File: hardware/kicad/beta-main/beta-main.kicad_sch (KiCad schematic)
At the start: 0 parts

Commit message: tweaks and added servo controller
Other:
- sheet CM5 ports: added 12V; removed none
- sheet PSU ports: added 12V; removed none
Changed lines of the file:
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@@
+	(wire
+		(pts
+			(xy 73.66 49.53) (xy 93.98 49.53)
+		)
+		(stroke
+			(width 0)
+			(type default)
+		)
+	)
 	(wire
 		(pts
@@
 			)
 		)
+		(pin "12V" output
+			(at 73.66 49.53 0)
+			(effects
+				(font
+					(size 1.27 1.27)
+				)
+				(justify right)
+			)
+		)
 		(instances
 			(project "beta-main"
@@
 			(effects
 				(font
+					(size 1.27 1.27)
+				)
+				(justify left)
+			)
+		)
+		(pin "12V" input
+			(at 93.98 49.53 180)
+			(effects
+				(font

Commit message: sync changes after meeting
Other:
- added sheet Servo Controller (servo_controller.kicad_sch)
- sheet CM5 ports: added UART3_RX, UART3_TX; removed none
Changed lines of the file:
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@@
 	(wire
 		(pts
-			(xy 68.58 69.85) (xy 68.58 72.39)
-		)
-		(stroke
-			(width 0)
-			(type default)
-		)
-	)
-	(wire
-		(pts
-			(xy 73.66 49.53) (xy 93.98 49.53)
-		)
-		(stroke
-			(width 0)
-			(type default)
-		)
-	)
-	(wire
-		(pts
-			(xy 73.66 57.15) (xy 93.98 57.15)
+			(xy 41.91 49.53) (xy 41.91 52.07)
+		)
+		(stroke
+			(width 0)
+			(type default)
+		)
+	)
+	(wire
+		(pts
+			(xy 46.99 36.83) (xy 49.53 36.83)
+		)
+		(stroke
+			(width 0)
+			(type default)
+		)
+	)
+	(wire
+		(pts
+			(xy 46.99 33.02) (xy 49.53 33.02)
+		)
+		(stroke
+			(width 0)
+			(type default)
+		)
+	)
+	(wire
+		(pts
+			(xy 46.99 29.21) (xy 49.53 29.21)
+		)
+		(stroke
+			(width 0)
+			(type default)
+		)
+	)
+	(wire
+		(pts
+			(xy 128.27 50.8) (xy 142.24 50.8)
+		)
+		(stroke
+			(width 0)
+			(type default)
+		)
+	)
+	(wire
+		(pts
+			(xy 128.27 54.61) (xy 142.24 54.61)
 		)
 		(stroke
@@
 		)
 	)
-	(wire
-		(pts
-			(xy 73.66 53.34) (xy 93.98 53.34)
-		)
-		(stroke
-			(width 0)
-			(type default)
+	(label "3V3"
+		(at 49.53 36.83 0)
+		(effects
+			(font
+				(size 1.27 1.27)
+			)
+			(justify left bottom)
+		)
+	)
+	(label "5V"
+		(at 49.53 33.02 0)
+		(effects
+			(font
+				(size 1.27 1.27)
+			)
+			(justify left bottom)
+		)
+	)
+	(label "12V"
+		(at 49.53 29.21 0)
+		(effects
+			(font
+				(size 1.27 1.27)
+			)
+			(justify left bottom)
 		)
 	)
@@
 	(symbol
 		(lib_id "power:GND")
-		(at 68.58 72.39 0)
+		(at 41.91 52.07 0)
 		(unit 1)
 		(exclude_from_sim no)
@@
 		(fields_autoplaced yes)
 		(property "Reference" "#PWR02"
-			(at 68.58 78.74 0)
+			(at 41.91 58.42 0)
 			(effects
 				(font
@@
 		)
 		(property "Value" "GND"
-			(at 68.58 77.47 0)
+			(at 41.91 57.15 0)
 			(effects
 				(font
@@
 		)
 		(property "Footprint" ""
-			(at 68.58 72.39 0)
+			(at 41.91 52.07 0)
 			(effects
 				(font
@@
 		)
 		(property "Datasheet" ""
-			(at 68.58 72.39 0)
+			(at 41.91 52.07 0)
 			(effects
 				(font
@@
 		)
 		(property "Description" "Power symbol creates a global label with name \"GND\" , ground"
-			(at 68.58 72.39 0)
+			(at 41.91 52.07 0)
 			(effects
 				(font
@@
 	)
 	(sheet
-		(at 46.99 45.72)
+		(at 20.32 25.4)
 		(size 26.67 24.13)
 		(exclude_from_sim no)
@@
 		)
 		(property "Sheetname" "PSU"
-			(at 46.99 45.0084 0)
+			(at 20.32 24.6884 0)
 			(effects
 				(font
@@
 		)
 		(property "Sheetfile" "psu.kicad_sch"
-			(at 46.99 70.4346 0)
+			(at 20.32 50.1146 0)
 			(effects
 				(font
@@
 		)
 		(pin "GND" passive
-			(at 68.58 69.85 270)
+			(at 41.91 49.53 270)
 			(effects
 				(font
@@
 		)
 		(pin "5V" output
-			(at 73.66 53.34 0)
+			(at 46.99 33.02 0)
 			(effects
 				(font
@@
 		)
 		(pin "3V3" output
-			(at 73.66 57.15 0)
+			(at 46.99 36.83 0)
 			(effects
 				(font
@@
 		)
 		(pin "12V" output
-			(at 73.66 49.53 0)
+			(at 46.99 29.21 0)
 			(effects
 				(font
@@
 			)
 		)
+		(pin "UART3_RX" input
+			(at 128.27 54.61 0)
+			(effects
+				(font
+					(size 1.27 1.27)
+				)
+				(justify right)
+			)
+		)
+		(pin "UART3_TX" input
+			(at 128.27 50.8 0)
+			(effects
+				(font
+					(size 1.27 1.27)
+				)
+				(justify right)
+			)
+		)
 		(instances
 			(project "beta-main"
@@
 				)
 			)
+		)
+	)
+	(sheet
+		(at 142.24 45.72)
+		(size 34.29 22.86)
+		(exclude_from_sim no)
+		(in_bom yes)
+		(on_board yes)
+		(dnp no)
+		(fields_autoplaced yes)
+		(stroke
+			(width 0.1524)
+			(type solid)
+		)
+		(fill
+			(color 0 0 0 0.0000)
+		)
+		(property "Sheetname" "Servo Controller"
+			(at 142.24 45.0084 0)
+			(effects
+				(font
+					(size 1.27 1.27)
+				)
+				(justify left bottom)
+			)
+		)
+		(property "Sheetfile" "servo_controller.kicad_sch"
+			(at 142.24 69.1646 0)
+			(effects
+				(font
+					(size 1.27 1.27)
+				)
+				(justify left top)
+			)
+		)
+		(pin "3V3" input
+			(at 142.24 64.77 180)
+			(effects
+				(font
+					(size 1.27 1.27)
+				)
+				(justify left)
+			)
+		)
+		(pin "12V" input
+			(at 142.24 62.23 180)
+			(effects
+				(font
+					(size 1.27 1.27)
+				)
+				(justify left)
+			)
+		)
+		(pin "GND" input
+			(at 170.18 68.58 270)
+			(effects
+				(font
+					(size 1.27 1.27)
+				)
+				(justify left)
+			)
+		)
+		(pin "UART_RX" input
+			(at 142.24 54.61 180)
+			(effects
+				(font
+					(size 1.27 1.27)
+				)
+				(justify left)
+			)
+		)
+		(pin "UART_TX" input
+			(at 142.24 50.8 180)
+			(effects
+				(font
+					(size 1.27 1.27)
+				)
+				(justify left)
+			)
+		)
+		(instances
+			(project "beta-main"
+				(path "/ec75fd42-4efa-4f32-b57e-76d632cb46f5"
+					(page "10")
+				)
+			)

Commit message: Wzmacniacz dodany
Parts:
- added U4: MAX98357A, Package_DFN_QFN:TQFN-16-1EP_3x3mm_P0.5mm_EP1.23x1.23mm, symbol Audio:MAX98357A
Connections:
- new net: U4.10 (OUTN), U4.9 (OUTP)
- new net: U4.11 (GND), U4.15 (GND), U4.3 (GND)
- new net: U4.7 (VDD), U4.8 (VDD)
- new net CM5/GPIO18: U4.16 (BCLK)
- new net CM5/GPIO19: U4.14 (LRCLK)
- new net CM5/GPIO21: U4.1 (DIN)
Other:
- sheet CM5 ports: added GPIO18, GPIO19, GPIO21; removed none
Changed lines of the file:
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@@
+	(wire
+		(pts
+			(xy 109.22 41.91) (xy 109.22 45.72)
+		)
+		(stroke
+			(width 0)
+			(type default)
+		)
+	)
 	(wire
 		(pts
@@
 	(wire
 		(pts
+			(xy 104.14 12.7) (xy 101.6 12.7)
+		)
+		(stroke
+			(width 0)
+			(type default)
+		)
+	)
+	(wire
+		(pts
 			(xy 46.99 33.02) (xy 49.53 33.02)
 		)
@@
 	(wire
 		(pts
+			(xy 106.68 38.1) (xy 106.68 41.91)
+		)
+		(stroke
+			(width 0)
+			(type default)
+		)
+	)
+	(wire
+		(pts
+			(xy 104.14 38.1) (xy 104.14 43.18)
+		)
+		(stroke
+			(width 0)
+			(type default)
+		)
+	)
+	(wire
+		(pts
+			(xy 101.6 38.1) (xy 101.6 45.72)
+		)
+		(stroke
+			(width 0)
+			(type default)
+		)
+	)
+	(wire
+		(pts
 			(xy 46.99 29.21) (xy 49.53 29.21)
 		)
@@
 	(wire
 		(pts
+			(xy 109.22 41.91) (xy 106.68 41.91)
+		)
+		(stroke
+			(width 0)
+			(type default)
+		)
+	)
+	(wire
+		(pts
 			(xy 128.27 50.8) (xy 142.24 50.8)
 		)
@@
 		(pts
 			(xy 128.27 54.61) (xy 142.24 54.61)
+		)
+		(stroke
+			(width 0)
+			(type default)
+		)
+	)
+	(wire
+		(pts
+			(xy 105.41 43.18) (xy 104.14 43.18)
+		)
+		(stroke
+			(width 0)
+			(type default)
+		)
+	)
+	(wire
+		(pts
+			(xy 105.41 43.18) (xy 105.41 45.72)
 		)
 		(stroke
@@
 			)
 			(justify left bottom)
+		)
+	)
+	(symbol
+		(lib_id "Audio:MAX98357A")
+		(at 109.22 25.4 90)
+		(unit 1)
+		(exclude_from_sim no)
+		(in_bom yes)
+		(on_board yes)
+		(dnp no)
+		(fields_autoplaced yes)
+		(property "Reference" "U4"
+			(at 92.71 19.9546 90)
+			(effects
+				(font
+					(size 1.27 1.27)
+				)
+			)
+		)
+		(property "Value" "MAX98357A"
+			(at 92.71 22.4946 90)
+			(effects
+				(font
+					(size 1.27 1.27)
+				)
+			)
+		)
+		(property "Footprint" "Package_DFN_QFN:TQFN-16-1EP_3x3mm_P0.5mm_EP1.23x1.23mm"
+			(at 111.76 26.67 0)
+			(effects
+				(font
+					(size 1.27 1.27)
+				)
+				(hide yes)
+			)
+		)
+		(property "Datasheet" "https://www.analog.com/media/en/technical-documentation/data-sheets/MAX98357A-MAX98357B.pdf"
+			(at 111.76 25.4 0)
+			(effects
+				(font
+					(size 1.27 1.27)
+				)
+				(hide yes)
+			)
+		)
+		(property "Description" "Mono DAC with amplifier, I2S, PCM, TDM, 32-bit, 96khz, 3.2W, TQFP-16"
+			(at 109.22 25.4 0)
+			(effects
+				(font
+					(size 1.27 1.27)
+				)
+				(hide yes)
+			)
+		)
+		(pin "10"
+		)
+		(pin "7"
+		)
+		(pin "17"
+		)
+		(pin "11"
+		)
+		(pin "5"
+		)
+		(pin "2"
+		)
+		(pin "15"
+		)
+		(pin "8"
+		)
+		(pin "9"
+		)
+		(pin "4"
+		)
+		(pin "14"
+		)
+		(pin "16"
+		)
+		(pin "1"
+		)
+		(pin "13"
+		)
+		(pin "12"
+		)
+		(pin "6"
+		)
+		(pin "3"
+		)
+		(instances
+			(project ""
+				(path "/ec75fd42-4efa-4f32-b57e-76d632cb46f5"
+					(reference "U4")
+					(unit 1)
+				)
+			)
 		)
 	)
@@
 			(effects
 				(font
+					(size 1.27 1.27)
+				)
+				(justify right)
+			)
+		)
+		(pin "GPIO18" input
+			(at 105.41 45.72 90)
+			(effects
+				(font
+					(size 1.27 1.27)
+				)
+				(justify right)
+			)
+		)
+		(pin "GPIO19" input
+			(at 109.22 45.72 90)
+			(effects
+				(font
+					(size 1.27 1.27)
+				)
+				(justify right)
+			)
+		)
+		(pin "GPIO21" input
+			(at 101.6 45.72 90)
+			(effects
+				(font

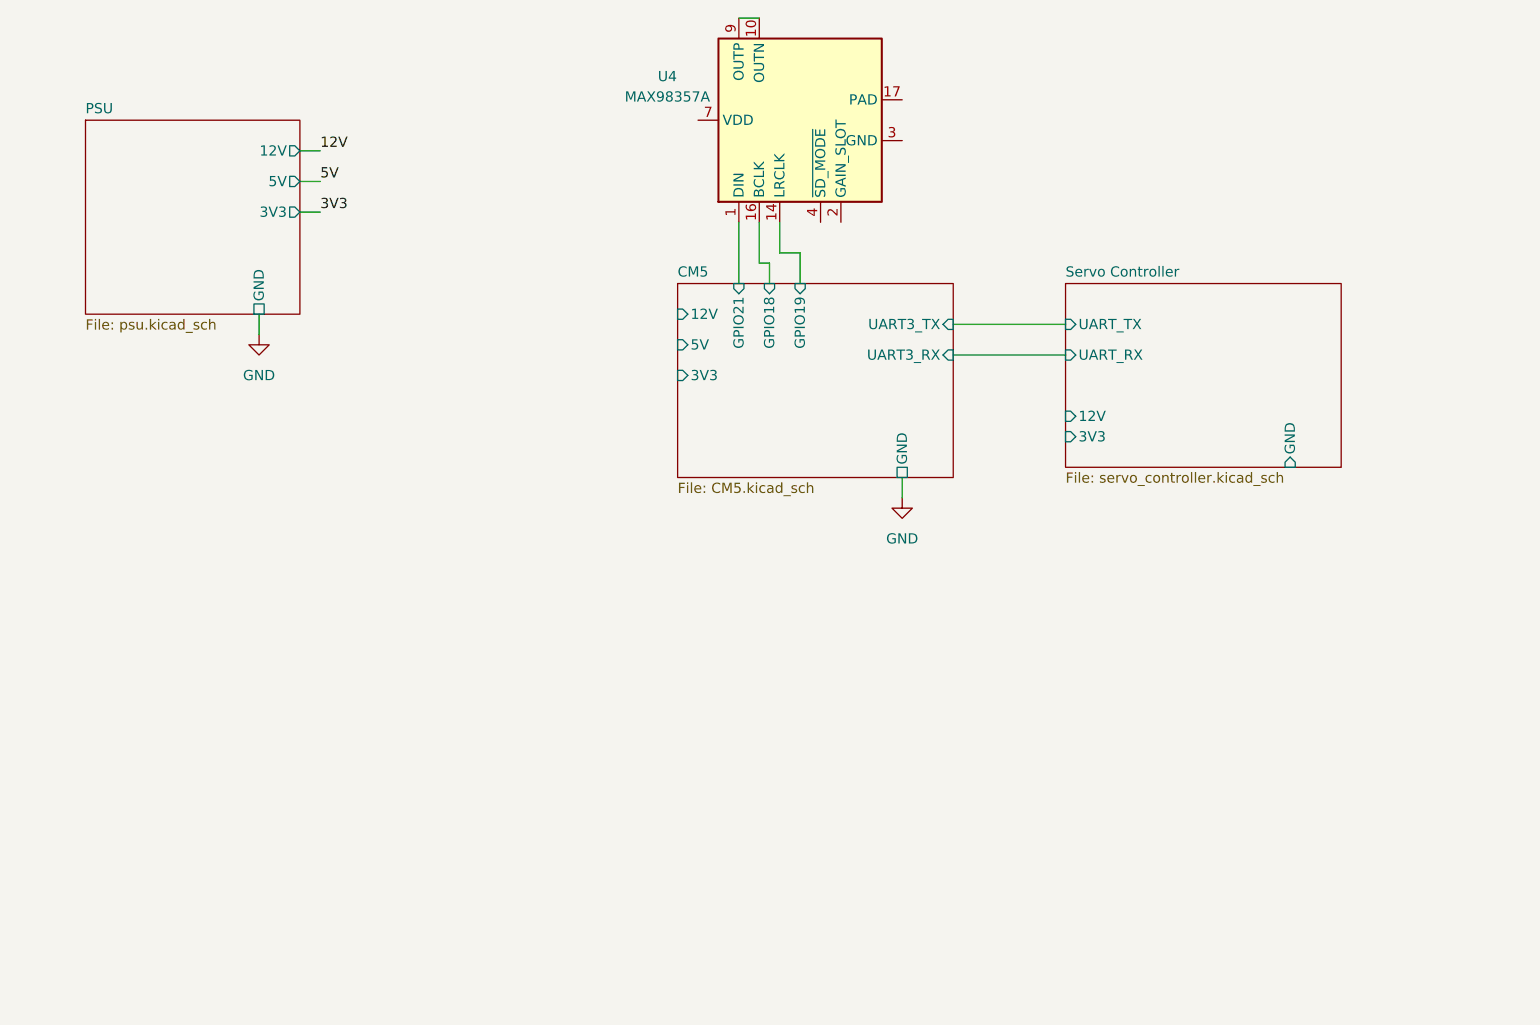
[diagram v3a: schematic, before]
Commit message: 5V and amplifier corrections
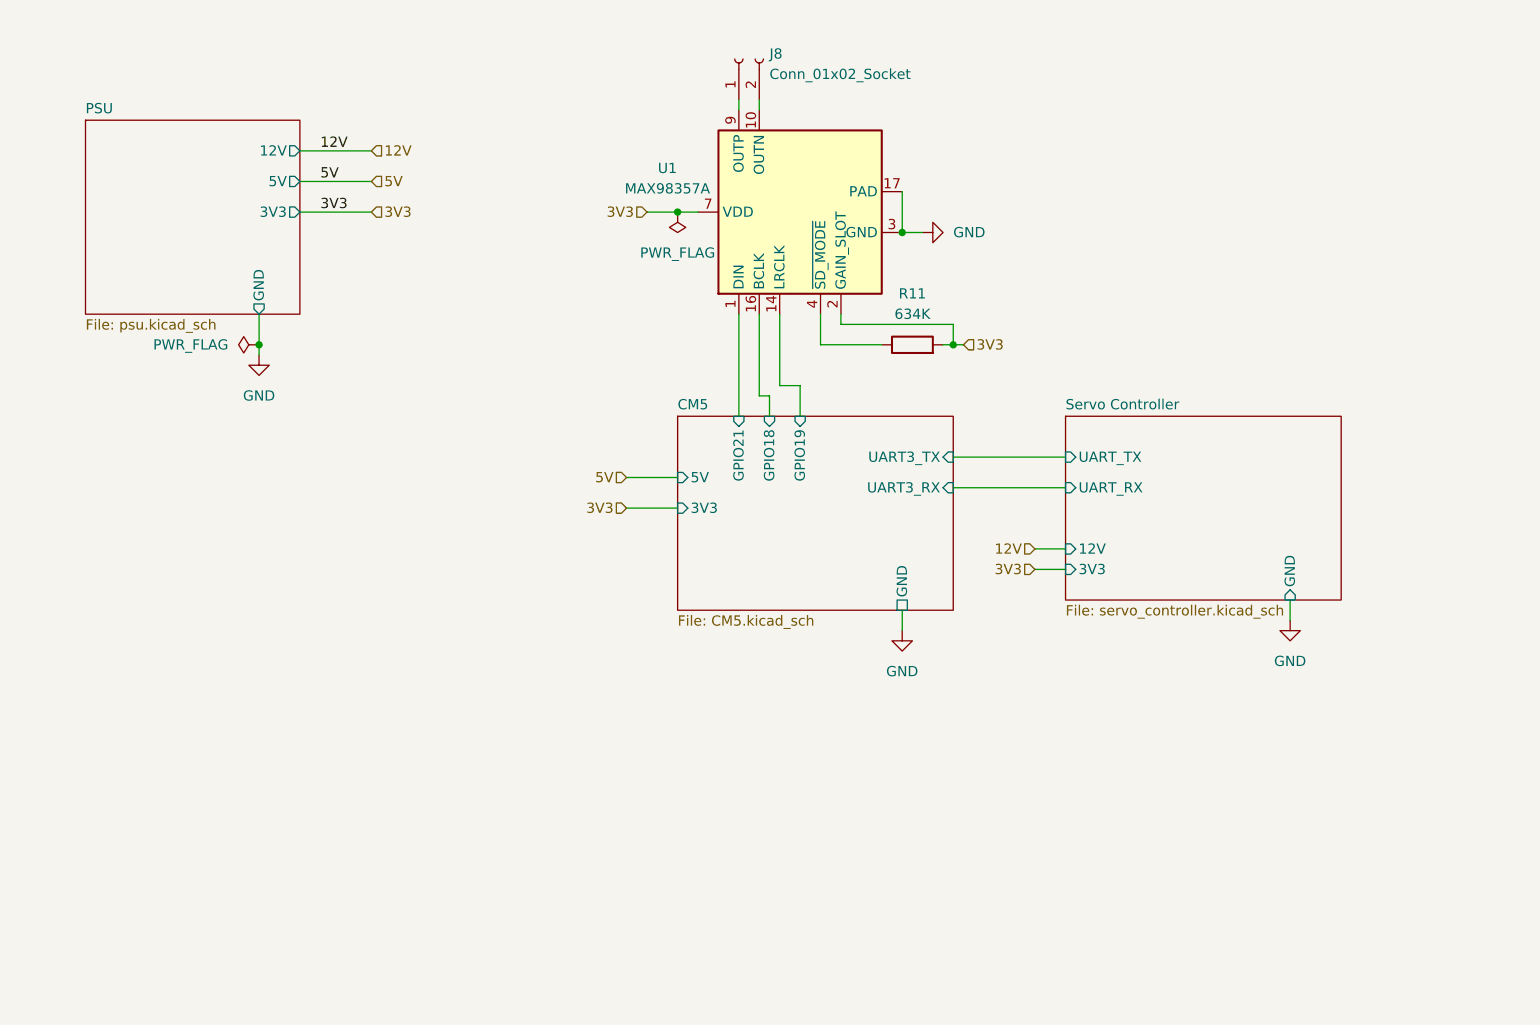
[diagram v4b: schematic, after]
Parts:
- added J8: Conn_01x02_Socket, symbol Connector:Conn_01x02_Socket
- added R11: 634K, symbol Device:R
- renumbered U4 to U1
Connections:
- net 3V3: now also U1.2 (GAIN_SLOT), U1.7 (VDD), U1.8 (VDD), R11.2
- net GND: now also U1.11 (GND), U1.15 (GND), U1.17 (PAD), U1.3 (GND)
- net at U1.10 (OUTN): now also J8.2 (Pin_2); no longer U1.9 (OUTP)
- net at U1.4 (~{SD_MODE}): now also R11.1
- new net: J8.1 (Pin_1), U1.9 (OUTP)
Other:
- sheet CM5 ports: added none; removed 12V
- moved on the sheet: U1

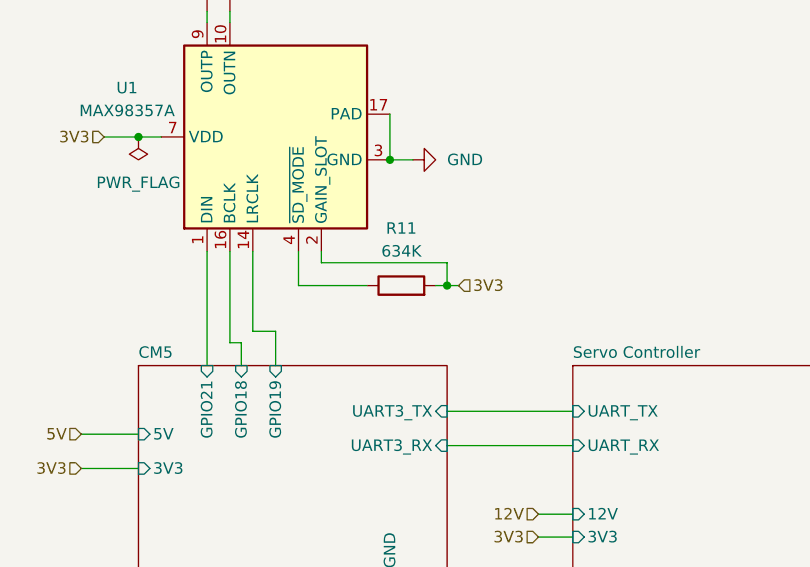
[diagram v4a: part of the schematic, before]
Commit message: Amplifier set for left channel only and god rid of all errors from ERC
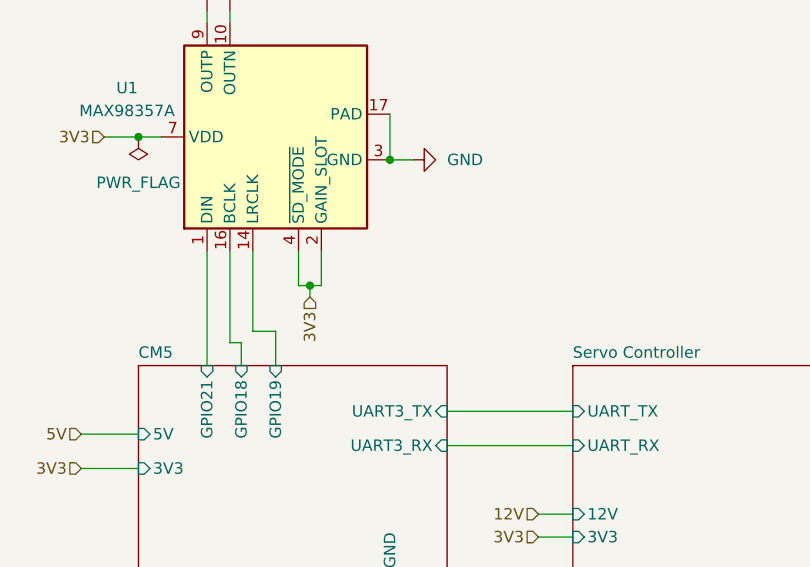
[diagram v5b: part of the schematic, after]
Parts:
- removed R11: 634K, symbol Device:R
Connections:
- net 3V3: now also U1.4 (~{SD_MODE})
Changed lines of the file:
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@@
 	)
 	(junction
-		(at 128.27 53.34)
+		(at 113.03 53.34)
 		(diameter 0)
 		(color 0 0 0 0)
@@
 	(wire
 		(pts
-			(xy 128.27 53.34) (xy 129.54 53.34)
-		)
-		(stroke
-			(width 0)
-			(type default)
-		)
-	)
-	(wire
-		(pts
 			(xy 46.99 33.02) (xy 55.88 33.02)
 		)
@@
 	(wire
 		(pts
-			(xy 128.27 50.8) (xy 128.27 53.34)
-		)
-		(stroke
-			(width 0)
-			(type default)
-		)
-	)
-	(wire
-		(pts
 			(xy 121.92 39.37) (xy 124.46 39.37)
 		)
@@
 	(wire
 		(pts
+			(xy 113.03 53.34) (xy 114.3 53.34)
+		)
+		(stroke
+			(width 0)
+			(type default)
+		)
+	)
+	(wire
+		(pts
 			(xy 138.43 78.74) (xy 142.24 78.74)
 		)
@@
 	(wire
 		(pts
+			(xy 113.03 53.34) (xy 113.03 54.61)
+		)
+		(stroke
+			(width 0)
+			(type default)
+		)
+	)
+	(wire
+		(pts
 			(xy 111.76 49.53) (xy 111.76 53.34)
 		)
@@
 	(wire
 		(pts
-			(xy 127 53.34) (xy 128.27 53.34)
-		)
-		(stroke
-			(width 0)
-			(type default)
-		)
-	)
-	(wire
-		(pts
 			(xy 46.99 29.21) (xy 55.88 29.21)
 		)
@@
 	(wire
 		(pts
+			(xy 111.76 53.34) (xy 113.03 53.34)
+		)
+		(stroke
+			(width 0)
+			(type default)
+		)
+	)
+	(wire
+		(pts
 			(xy 109.22 58.42) (xy 106.68 58.42)
 		)
@@
 	(wire
 		(pts
-			(xy 114.3 50.8) (xy 128.27 50.8)
-		)
-		(stroke
-			(width 0)
-			(type default)
-		)
-	)
-	(wire
-		(pts
 			(xy 121.92 34.29) (xy 121.92 39.37)
 		)
@@
 	(wire
 		(pts
-			(xy 119.38 53.34) (xy 111.76 53.34)
-		)
-		(stroke
-			(width 0)
-			(type default)
-		)
-	)
-	(wire
-		(pts
 			(xy 128.27 67.31) (xy 142.24 67.31)
 		)
@@
 	(wire
 		(pts
-			(xy 114.3 50.8) (xy 114.3 49.53)
+			(xy 114.3 49.53) (xy 114.3 53.34)
 		)
 		(stroke
@@
 	(hierarchical_label "3V3"
 		(shape input)
-		(at 129.54 53.34 0)
-		(effects
-			(font
-				(size 1.27 1.27)
-			)
-			(justify left)
+		(at 113.03 54.61 270)
+		(effects
+			(font
+				(size 1.27 1.27)
+			)
+			(justify right)
 		)
 	)
@@
 					(unit 1)
 				)
-			)
-		)
-	)
-	(symbol
-		(lib_id "Device:R")
-		(at 123.19 53.34 90)
-		(unit 1)
-		(exclude_from_sim no)
-		(in_bom yes)
-		(on_board yes)
-		(dnp no)
-		(fields_autoplaced yes)
-		(property "Reference" "R11"
-			(at 123.19 46.99 90)
-			(effects
-				(font
-					(size 1.27 1.27)
-				)
-			)
-		)
-		(property "Value" "634K"
-			(at 123.19 49.53 90)
-			(effects
-				(font
-					(size 1.27 1.27)
-				)
-			)
-		)
-		(property "Footprint" ""
-			(at 123.19 55.118 90)
-			(effects
-				(font
-					(size 1.27 1.27)
-				)
-				(hide yes)
-			)
-		)
-		(property "Datasheet" "~"
-			(at 123.19 53.34 0)
-			(effects
-				(font
-					(size 1.27 1.27)
-				)
-				(hide yes)
-			)
-		)
-		(property "Description" "Resistor"
-			(at 123.19 53.34 0)
-			(effects
-				(font
-					(size 1.27 1.27)
-				)
-				(hide yes)
-			)
-		)
-		(pin "1"
-		)
-		(pin "2"
-		)
-		(instances
-			(project ""
-				(path "/ec75fd42-4efa-4f32-b57e-76d632cb46f5"
-					(reference "R11")
-					(unit 1)
-				)
